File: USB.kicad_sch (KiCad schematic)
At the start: 15 parts, among them J1 USB_B_Mini, U3 FT4232H, Y1 12MHz

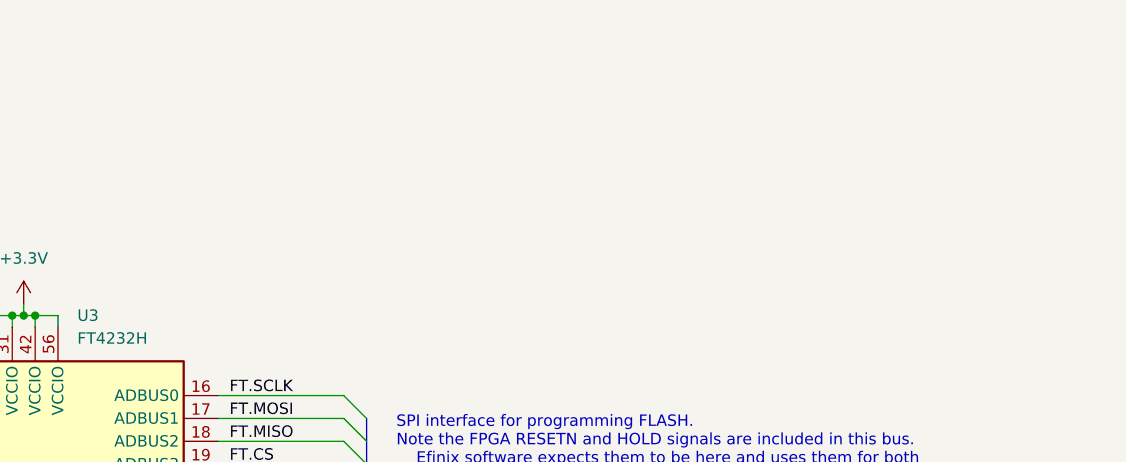
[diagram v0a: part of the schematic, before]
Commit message: Added ADC
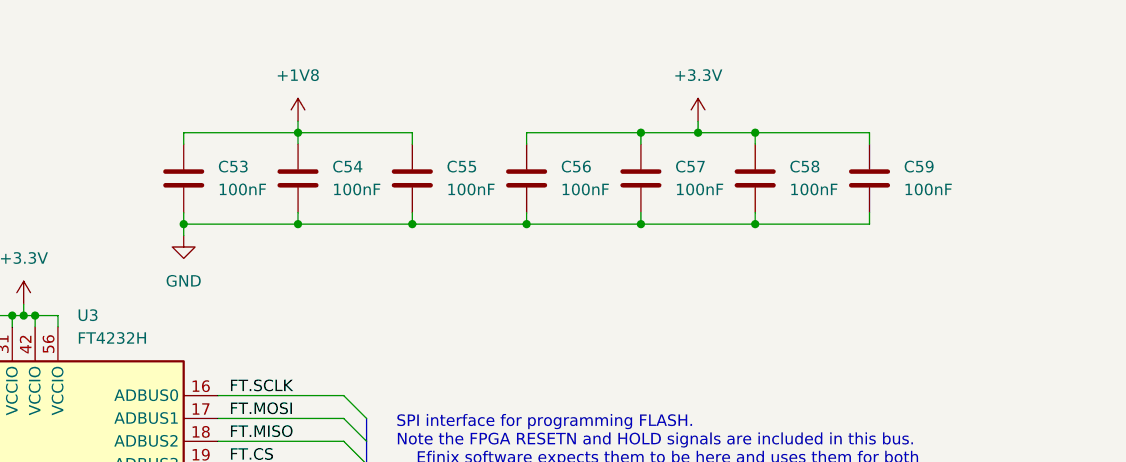
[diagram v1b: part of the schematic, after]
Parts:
- added C53, C54, C55, C56, C57, C58, C59: 100nF, Capacitor_SMD:C_0603_1608Metric, symbol Device:C
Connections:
- net +1V8: now also C53.1, C54.1, C55.1
- net +3.3V: now also C56.1, C57.1, C58.1, C59.1
- net GND: now also C53.2, C54.2, C55.2, C56.2, C57.2, C58.2, C59.2

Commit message: Added SRAM and removed old ADC
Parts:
- added C49: 100nF, Capacitor_SMD:C_0603_1608Metric, symbol Device:C
- added R64: 2k, Resistor_SMD:R_0603_1608Metric, symbol Device:R_US
- added R65, R66, R67: 10k, Resistor_SMD:R_0603_1608Metric, symbol Device:R_US
- added U8: 93AAxxBT-xOT, Package_TO_SOT_SMD:SOT-23-6, symbol Memory_EEPROM:93AAxxBT-xOT
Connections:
- net +3.3V: now also C49.1, R65.1, R66.1, R67.1, U8.6 (Vcc)
- net GND: now also C49.2, U8.2 (Vss)
- net EEDATA: now reaches U3.61 (EEDATA)
- net EEDATA: now also R64.1, R66.2, U8.3 (DI)
- net EECLK: now reaches U3.62 (EECLK)
- net EECLK: now also R65.2, U8.4 (CLK)
- net EECS: now reaches U3.63 (EECS)
- net EECS: now also R67.2, U8.5 (CS)
- new net: R64.2, U8.1 (DO)
- no-connect marks 17 -> 14
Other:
- note added: "EEPROM (optional)"

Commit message: Initial design
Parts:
- added R72: 1k, Resistor_SMD:R_0603_1608Metric, symbol Device:R_US
- added TP1, TP10, TP11, TP12, TP13, TP14, TP2, TP3, TP4, TP5, TP6, TP7, TP8, TP9: TestPoint, TestPoint:TestPoint_Pad_D2.0mm, symbol Connector:TestPoint
- C10, C11, C7: Digikey PN (none) -> 1276-1044-1-ND; Unit Cost (none) -> 0.044
- C12, C13, C49, C53, C54, C55, C56, C57, C58, C59: Digikey PN (none) -> 1276-6854-1-ND; Unit Cost (none) -> 0.055
- C8, C9: value 27pF -> 20pF; Digikey PN (none) -> 1276-1187-1-ND; Unit Cost (none) -> 0.10
- FB1, FB2: Digikey PN (none) -> 490-1014-1-ND; Unit Cost (none) -> 0.1
- J1: footprint (none) -> Connector_USB:USB_Mini-B_Wuerth_65100516121_Horizontal; Digikey PN (none) -> 151-1206-1-ND; Unit Cost (none) -> 0.61
- JP1: footprint (none) -> Jumper:SolderJumper-2_P1.3mm_Open_RoundedPad1.0x1.5mm
- R13: Digikey PN (none) -> 311-12.0KHRCT-ND; Unit Cost (none) -> 0.10
- R14: Digikey PN (none) -> 311-1.00KHRCT-ND; Unit Cost (none) -> 0.025
- R64: value 2k -> 1k; Digikey PN (none) -> 311-1.00KHRCT-ND; Unit Cost (none) -> 0.025
- R65, R66, R67: Digikey PN (none) -> 311-10KLDCT-ND; Unit Cost (none) -> 0.028
- U3: Unit Cost (none) -> 10.0
- U8: Digikey PN (none) -> 93AA56BT-I/OTCT-ND; Unit Cost (none) -> 0.32
- Y1: footprint (none) -> Crystal:Crystal_SMD_ECS_CSM3X-2Pin_7.6x4.1mm; Digikey PN (none) -> XC1787CT-ND; Unit Cost (none) -> 0.37
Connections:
- net +1V8: now also TP3.1
- net BB0: now also TP7.1
- net BB1: now also TP8.1
- net BB2: now also TP9.1
- net BB3: now also TP10.1
- net BB4: now also TP11.1
- net BB5: now also TP12.1
- net BB6: now also TP13.1
- net BB7: now also TP14.1
- net EECLK: now also TP5.1
- net EECS: now also TP4.1
- net EEDATA: now also R72.2, TP6.1; no longer R64.1
- net at C10.1, C12.1, FB1.2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: now also TP1.1
- net at C11.1, C13.1, FB2.2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: now also TP2.1
- new net: R64.1, R72.1
- no-connect marks 14 -> 15

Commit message: Added ethernet
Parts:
- TP1, TP10, TP11, TP12, TP13, TP14, TP2, TP3, TP4, TP5, TP6, TP7, TP8, TP9: now left out of the parts list
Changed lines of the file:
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@@
 		(body_style 1)
 		(exclude_from_sim no)
-		(in_bom yes)
+		(in_bom no)
 		(on_board yes)
 		(in_pos_files yes)
@@
 		(body_style 1)
 		(exclude_from_sim no)
-		(in_bom yes)
+		(in_bom no)
 		(on_board yes)
 		(in_pos_files yes)
@@
 		(body_style 1)
 		(exclude_from_sim no)
-		(in_bom yes)
+		(in_bom no)
 		(on_board yes)
 		(in_pos_files yes)
@@
 		(body_style 1)
 		(exclude_from_sim no)
-		(in_bom yes)
+		(in_bom no)
 		(on_board yes)
 		(in_pos_files yes)
@@
 		(body_style 1)
 		(exclude_from_sim no)
-		(in_bom yes)
+		(in_bom no)
 		(on_board yes)
 		(in_pos_files yes)
@@
 		(body_style 1)
 		(exclude_from_sim no)
-		(in_bom yes)
+		(in_bom no)
 		(on_board yes)
 		(in_pos_files yes)
@@
 		(body_style 1)
 		(exclude_from_sim no)
-		(in_bom yes)
+		(in_bom no)
 		(on_board yes)
 		(in_pos_files yes)
@@
 		(body_style 1)
 		(exclude_from_sim no)
-		(in_bom yes)
+		(in_bom no)
 		(on_board yes)
 		(in_pos_files yes)
@@
 		(body_style 1)
 		(exclude_from_sim no)
-		(in_bom yes)
+		(in_bom no)
 		(on_board yes)
 		(in_pos_files yes)
@@
 		(body_style 1)
 		(exclude_from_sim no)
-		(in_bom yes)
+		(in_bom no)
 		(on_board yes)
 		(in_pos_files yes)
@@
 		(body_style 1)
 		(exclude_from_sim no)
-		(in_bom yes)
+		(in_bom no)
 		(on_board yes)
 		(in_pos_files yes)
@@
 		(body_style 1)
 		(exclude_from_sim no)
-		(in_bom yes)
+		(in_bom no)
 		(on_board yes)
 		(in_pos_files yes)
@@
 		(body_style 1)
 		(exclude_from_sim no)
-		(in_bom yes)
+		(in_bom no)
 		(on_board yes)
 		(in_pos_files yes)
@@
 		(body_style 1)
 		(exclude_from_sim no)
-		(in_bom yes)
+		(in_bom no)
 		(on_board yes)
 		(in_pos_files yes)

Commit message: Cleanup
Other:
- title: (none) -> USB
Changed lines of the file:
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@@
 	(generator_version "10.0")
 	(paper "A4")
+	(title_block
+		(title "USB")
+		(date "2026-09-19")
+	)
 	(rectangle
 		(start 16.51 125.73)

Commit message: Annotated schematic
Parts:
- renumbered C49 to C32, C10 to C33, C9 to C34, C11 to C35, C8 to C36, C7 to C37, C12 to C38, C13 to C39, C53 to C40, C54 to C41, C55 to C42, C56 to C43, C57 to C44, C58 to C45, C59 to C46, JP1 to JP2, R67 to R42, R64 to R43, R65 to R44, R72 to R45, R66 to R46, R13 to R47, R14 to R48, TP4 to TP14, TP5 to TP15, TP6 to TP16, TP3 to TP17, TP2 to TP18, TP1 to TP19, TP7 to TP20, TP8 to TP21, TP9 to TP22, TP10 to TP23, TP11 to TP24, TP12 to TP25, TP13 to TP26, TP14 to TP27, U8 to U6, U3 to U7, Y1 to Y2

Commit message: Started module-level layout
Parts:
- removed Y2: 12MHz, Crystal:Crystal_SMD_ECS_CSM3X-2Pin_7.6x4.1mm, symbol Device:Crystal_Small
- added C33: 1uF, Capacitor_SMD:C_0603_1608Metric, symbol Device:C
- added F1: Fuse, Fuse:Fuse_0603_1608Metric, symbol Device:Fuse
- added R47, R48: 10, Resistor_SMD:R_0603_1608Metric, symbol Device:R_US
- added TP14: TestPoint, TestPoint:TestPoint_Pad_D1.0mm, symbol Connector:TestPoint
- added U7: USBLC6-2SC6, Package_TO_SOT_SMD:SOT-23-6, symbol Power_Protection:USBLC6-2SC6
- added Y2: Crystal_GND24, Crystal:Crystal_SMD_3225-4Pin_3.2x2.5mm, symbol Device:Crystal_GND24
- C35: renamed from C34; value 20pF -> 10pF; Digikey PN 1276-1187-1-ND -> 1276-2149-1-ND
- C37: renamed from C36; value 20pF -> 10pF; Digikey PN 1276-1187-1-ND -> 1276-2149-1-ND
- TP15: renamed from TP14; footprint TestPoint:TestPoint_Pad_D2.0mm -> TestPoint:TestPoint_Pad_D1.0mm
- TP16: renamed from TP15; footprint TestPoint:TestPoint_Pad_D2.0mm -> TestPoint:TestPoint_Pad_D1.0mm
- TP17: renamed from TP16; footprint TestPoint:TestPoint_Pad_D2.0mm -> TestPoint:TestPoint_Pad_D1.0mm
- TP18: renamed from TP17; footprint TestPoint:TestPoint_Pad_D2.0mm -> TestPoint:TestPoint_Pad_D1.0mm
- TP19: renamed from TP18; footprint TestPoint:TestPoint_Pad_D2.0mm -> TestPoint:TestPoint_Pad_D1.0mm
- TP20: renamed from TP19; footprint TestPoint:TestPoint_Pad_D2.0mm -> TestPoint:TestPoint_Pad_D1.0mm
- TP21: renamed from TP20; footprint TestPoint:TestPoint_Pad_D2.0mm -> TestPoint:TestPoint_Pad_D1.0mm
- TP22: renamed from TP21; footprint TestPoint:TestPoint_Pad_D2.0mm -> TestPoint:TestPoint_Pad_D1.0mm
- TP23: renamed from TP22; footprint TestPoint:TestPoint_Pad_D2.0mm -> TestPoint:TestPoint_Pad_D1.0mm
- TP24: renamed from TP23; footprint TestPoint:TestPoint_Pad_D2.0mm -> TestPoint:TestPoint_Pad_D1.0mm
- TP25: renamed from TP24; footprint TestPoint:TestPoint_Pad_D2.0mm -> TestPoint:TestPoint_Pad_D1.0mm
- TP26: renamed from TP25; footprint TestPoint:TestPoint_Pad_D2.0mm -> TestPoint:TestPoint_Pad_D1.0mm
- TP27: renamed from TP26; footprint TestPoint:TestPoint_Pad_D2.0mm -> TestPoint:TestPoint_Pad_D1.0mm
- TP28: renamed from TP27; footprint TestPoint:TestPoint_Pad_D2.0mm -> TestPoint:TestPoint_Pad_D1.0mm
- renumbered C33 to C34, C35 to C36, C37 to C38, C38 to C39, C39 to C40, C40 to C41, C41 to C42, C42 to C43, C43 to C44, C44 to C45, C45 to C46, C46 to C47, R47 to R49, R48 to R50, U7 to U8
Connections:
- net EEDATA: no longer R46.2
- net GND: now also C33.2, U7.2 (GND), Y2.2 (G), Y2.4 (G)
- net USB_D+: now also U7.3 (I/O2); no longer U8.8 (DP)
- net USB_D-: now also U7.1 (I/O1); no longer U8.7 (DM)
- net VBUS: now also C33.1, F1.1, U7.5 (VBUS); no longer J1.1 (VBUS)
- net at C37.1, U8.3 (OSCO): now also Y2.3
- net at C35.1, U8.2 (OSCI): now also Y2.1
- net at R43.2, U6.1 (DO): now also R46.2, TP14.1
- new net: R48.2, U7.4 (I/O2)
- new net: R47.2, U7.6 (I/O1)
- new net: F1.2, J1.1 (VBUS)
- new net USB_ESD_D+: R48.1, U8.8 (DP)
- new net USB_ESD_D-: R47.1, U8.7 (DM)
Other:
- moved on the sheet: C32, J1, JP2, R42, R43, R44, R45, U6

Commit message: Routing done
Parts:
- removed J1: USB_B_Mini, Connector_USB:USB_Mini-B_Wuerth_65100516121_Horizontal, symbol Connector:USB_B_Mini
- removed JP2: SolderJumper_2_Open, Jumper:SolderJumper-2_P1.3mm_Open_RoundedPad1.0x1.5mm, symbol Jumper:SolderJumper_2_Open
- removed TP15, TP16, TP17, TP19, TP20, TP21, TP22, TP23, TP24, TP25, TP26, TP27, TP28: TestPoint, TestPoint:TestPoint_Pad_D1.0mm, symbol Connector:TestPoint
- added J1: USB_C_Receptacle_USB2.0_16P, Connector_USB:USB_C_Receptacle_GCT_USB4105-xx-A_16P_TopMnt_Horizontal, symbol Connector:USB_C_Receptacle_USB2.0_16P
- added R45, R46: 5.1k, Resistor_SMD:R_0603_1608Metric, symbol Device:R_US
- renumbered R45 to R47, R46 to R48, R47 to R49, R48 to R50, R49 to R89, R50 to R90
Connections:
- net GND: now also J1.A1 (GND), J1.A12 (GND), J1.B1 (GND), J1.B12 (GND), J1.SH (SHIELD), R45.1, R46.2
- net USB_D+: now also J1.A6 (D+), J1.B6 (D+)
- net USB_D-: now also J1.A7 (D-), J1.B7 (D-)
- net at F1.2: now also J1.A4 (VBUS), J1.A9 (VBUS), J1.B4 (VBUS), J1.B9 (VBUS)
- new net: J1.A5 (CC1), R45.2
- new net: J1.B5 (CC2), R46.1
- no-connect marks 15 -> 16
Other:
- moved on the sheet: C33, F1
